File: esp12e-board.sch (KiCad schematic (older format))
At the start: 9 parts

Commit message: First version sent to fab
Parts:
- removed J?: Conn_02x05_Odd_Even, symbol Connector_Generic:Conn_02x05_Odd_Even
- removed J?: 5V AUX, Connector_PinSocket_2.54mm:PinSocket_1x02_P2.54mm_Vertical, symbol Connector:Conn_01x02_Female
- removed SW?: SW_Push, symbol Switch:SW_Push
- added J1: Header, Connector_PinHeader_2.54mm:PinHeader_2x08_P2.54mm_Vertical, symbol Connector_Generic:Conn_02x08_Odd_Even
- U2: renamed from U?; footprint (none) -> ESP8266:ESP-12E_SMD
- gave numbers to parts that had none: 5
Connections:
- wire segments 47 -> 55
- no-connect marks 11 -> 9

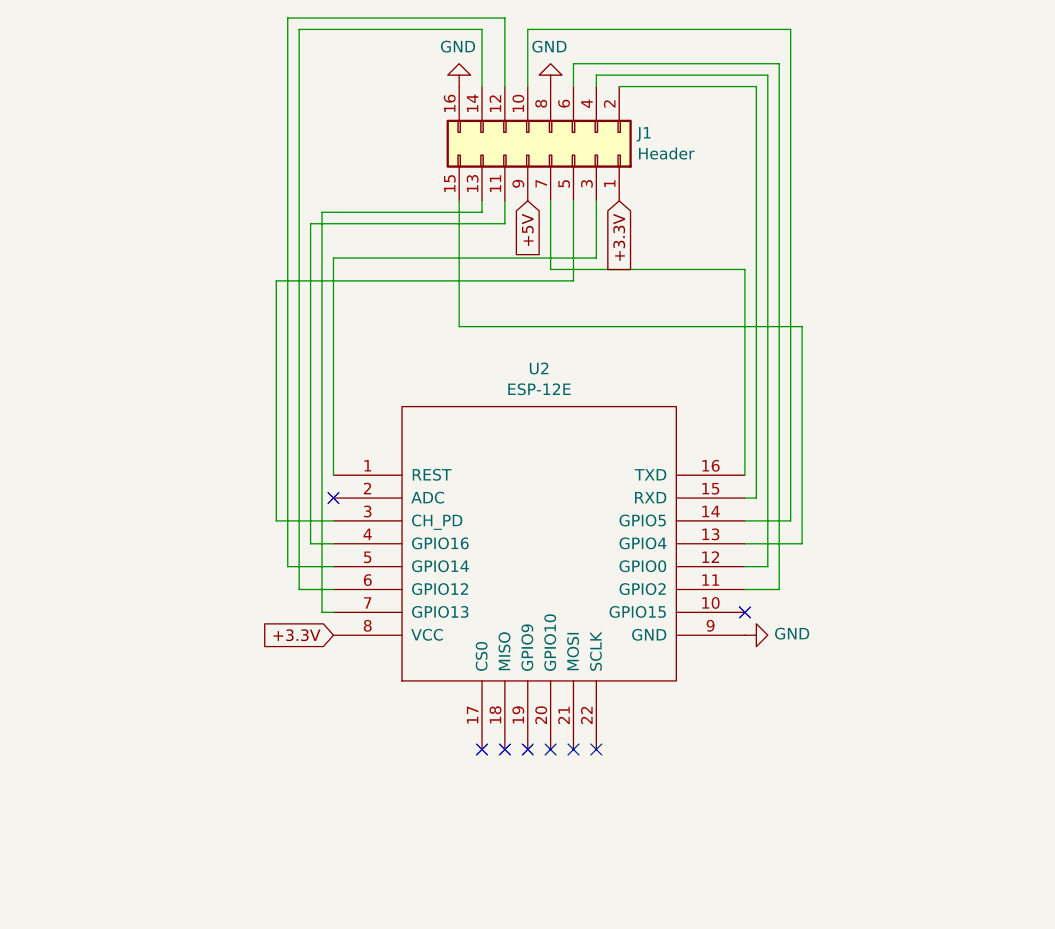
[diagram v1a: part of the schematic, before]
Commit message: adds necessary pull up/down resistors to pins to be able to boot
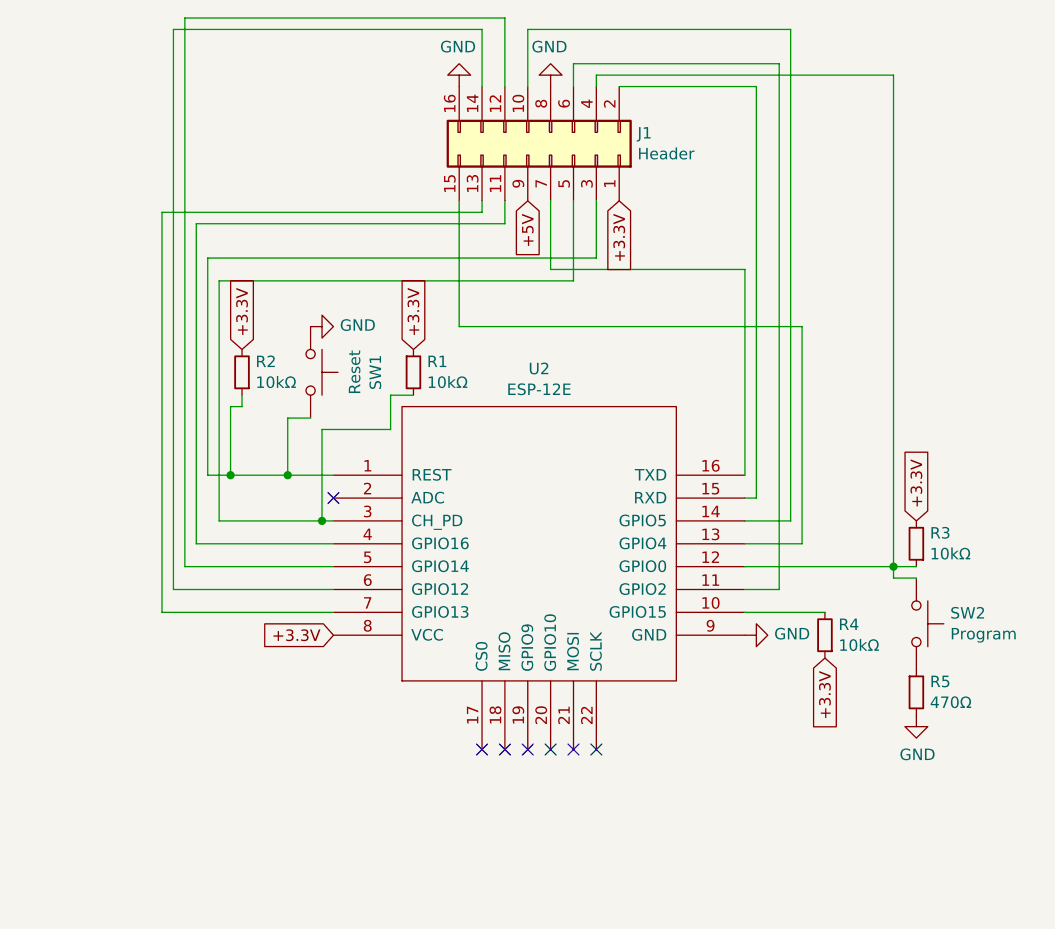
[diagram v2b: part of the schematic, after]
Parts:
- added R1, R2, R3, R4: 10kΩ, Resistor_SMD:R_0805_2012Metric_Pad1.15x1.40mm_HandSolder, symbol Device:R_Small
- added R5: 470Ω, Resistor_SMD:R_0805_2012Metric_Pad1.15x1.40mm_HandSolder, symbol Device:R_Small
- added SW1: Reset, Jumper:SolderJumper-2_P1.3mm_Open_RoundedPad1.0x1.5mm, symbol Switch:SW_Push
- added SW2: Program, Jumper:SolderJumper-2_P1.3mm_Open_RoundedPad1.0x1.5mm, symbol Switch:SW_Push
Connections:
- net +3.3V: now also R1.1, R2.2, R3.2, R4.1
- net GND: now also R5.2, SW1.1
- net at J1.3 (Pin_3), U2.1 (REST): now also R2.1, SW1.2
- net at U2.10 (GPIO15): now also R4.2
- net at J1.4 (Pin_4), U2.12 (GPIO0): now also R3.1, SW2.1
- net at J1.5 (Pin_5), U2.3 (CH_PD): now also R1.2
- new net: R5.1, SW2.2
- no-connect marks 9 -> 8
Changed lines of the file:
@@
 EESchema Schematic File Version 4
+LIBS:esp12e-board-cache
 EELAYER 30 0
 EELAYER END
@@
 NoConn ~ 5950 5150
 NoConn ~ 5850 5150
-NoConn ~ 6600 4550
 $Comp
 L ESP8266:ESP-12E U2
@@
 Wire Wire Line
 	6650 4050 6650 2250
-Wire Wire Line
-	4800 4250 4700 4250
 $Comp
 L power:GND #PWR01
@@
 +5V
 Wire Wire Line
-	4750 4550 4750 2800
-Wire Wire Line
-	4750 2800 5450 2800
-Wire Wire Line
 	5450 2800 5450 2750
 Wire Wire Line
-	4750 4550 4800 4550
-Wire Wire Line
 	5550 2750 5550 2850
 Wire Wire Line
-	5550 2850 4700 2850
-Wire Wire Line
-	4700 2850 4700 4250
-Wire Wire Line
 	6600 3050 5750 3050
 Wire Wire Line
@@
 	5450 2000 5450 2250
 Wire Wire Line
-	4650 2000 5450 2000
-Wire Wire Line
-	4650 4450 4650 2000
-Wire Wire Line
-	4800 4450 4650 4450
-Wire Wire Line
 	5550 1950 5550 2250
 Wire Wire Line
-	4600 1950 5550 1950
-Wire Wire Line
-	4600 4350 4600 1950
-Wire Wire Line
-	4800 4350 4600 4350
-Wire Wire Line
-	6600 4350 6700 4350
-Wire Wire Line
-	6700 4350 6700 2200
-Wire Wire Line
-	6700 2200 5950 2200
-Wire Wire Line
 	5950 2200 5950 2250
 Wire Wire Line
@@
 	5850 2150 5850 2250
 Wire Wire Line
-	4800 3950 4800 3000
-Wire Wire Line
-	4800 3000 5950 3000
-Wire Wire Line
 	5950 3000 5950 2750
 Wire Wire Line
-	4800 4150 4550 4150
-Wire Wire Line
-	4550 4150 4550 3100
-Wire Wire Line
-	4550 3100 5850 3100
-Wire Wire Line
 	5850 3100 5850 2750
 Wire Wire Line
@@
 Wire Wire Line
 	5350 3300 5350 2750
+$Comp
+L Device:R_Small R4
+U 1 1 5E563141
+P 6950 4650
+F 0 "R4" H 6891 4604 50  0000 R CNN
+F 1 "10kΩ" H 6891 4695 50  0000 R CNN
+F 2 "Resistor_SMD:R_0805_2012Metric_Pad1.15x1.40mm_HandSolder" H 6950 4650 50  0001 C CNN
+F 3 "~" H 6950 4650 50  0001 C CNN
+	1    6950 4650
+	-1   0    0    1
+$EndComp
+$Comp
+L Device:R_Small R3
+U 1 1 5E56376D
+P 7350 4250
+F 0 "R3" H 7291 4204 50  0000 R CNN
+F 1 "10kΩ" H 7291 4295 50  0000 R CNN
+F 2 "Resistor_SMD:R_0805_2012Metric_Pad1.15x1.40mm_HandSolder" H 7350 4250 50  0001 C CNN
+F 3 "~" H 7350 4250 50  0001 C CNN
+	1    7350 4250
+	-1   0    0    1
+$EndComp
+$Comp
+L Device:R_Small R2
+U 1 1 5E563C3F
+P 4400 3500
+F 0 "R2" H 4341 3454 50  0000 R CNN
+F 1 "10kΩ" H 4341 3545 50  0000 R CNN
+F 2 "Resistor_SMD:R_0805_2012Metric_Pad1.15x1.40mm_HandSolder" H 4400 3500 50  0001 C CNN
+F 3 "~" H 4400 3500 50  0001 C CNN
+	1    4400 3500
+	-1   0    0    1
+$EndComp
+Wire Wire Line
+	6600 4550 6950 4550
+Text GLabel 4400 3400 1    50   Input ~ 0
++3.3V
+Text GLabel 6950 4750 3    50   Input ~ 0
++3.3V
+Text GLabel 7350 4150 1    50   Input ~ 0
++3.3V
+Wire Wire Line
+	5950 2200 7250 2200
+Wire Wire Line
+	7250 4350 7250 2200
+$Comp
+L Device:R_Small R5
+U 1 1 5E5A201A
+P 7350 4900
+F 0 "R5" H 7409 4946 50  0000 L CNN
+F 1 "470Ω" H 7409 4855 50  0000 L CNN
+F 2 "Resistor_SMD:R_0805_2012Metric_Pad1.15x1.40mm_HandSolder" H 7350 4900 50  0001 C CNN
+F 3 "~" H 7350 4900 50  0001 C CNN
+	1    7350 4900
+	1    0    0    -1
+$EndComp
+Wire Wire Line
+	6600 4350 7250 4350
+Wire Wire Line
+	7250 4350 7350 4350
+Connection ~ 7250 4350
+Wire Wire Line
+	7250 4350 7250 4400
+Wire Wire Line
+	7250 4400 7350 4400
+$Comp
+L Switch:SW_Push SW2
+U 1 1 5E5AA7EE
+P 7350 4600
+F 0 "SW2" V 7304 4748 50  0000 L CNN
+F 1 "Program" V 7395 4748 50  0000 L CNN
+F 2 "Jumper:SolderJumper-2_P1.3mm_Open_RoundedPad1.0x1.5mm" H 7350 4800 50  0001 C CNN
+F 3 "~" H 7350 4800 50  0001 C CNN
+	1    7350 4600
+	0    1    1    0
+$EndComp
+$Comp
+L power:GND #PWR03
+U 1 1 5E5ADADC
+P 7350 5000
+F 0 "#PWR03" H 7350 4750 50  0001 C CNN
+F 1 "GND" H 7355 4827 50  0000 C CNN
+F 2 "" H 7350 5000 50  0001 C CNN
+F 3 "" H 7350 5000 50  0001 C CNN
+	1    7350 5000
+	1    0    0    -1
+$EndComp
+$Comp
+L Switch:SW_Push SW1
+U 1 1 5E5AE838
+P 4700 3500
+F 0 "SW1" H 4700 3785 50  0000 C CNN
+F 1 "Reset" H 4700 3694 50  0000 C CNN
+F 2 "Jumper:SolderJumper-2_P1.3mm_Open_RoundedPad1.0x1.5mm" H 4700 3700 50  0001 C CNN
+F 3 "~" H 4700 3700 50  0001 C CNN
+	1    4700 3500
+	0    1    1    0
+$EndComp
+Wire Wire Line
+	4750 4150 4800 4150
+Connection ~ 4750 4150
+Text GLabel 5150 3400 1    50   Input ~ 0
++3.3V
+$Comp
+L Device:R_Small R1
+U 1 1 5E5639CE
+P 5150 3500
+F 0 "R1" H 5209 3546 50  0000 L CNN
+F 1 "10kΩ" H 5209 3455 50  0000 L CNN
+F 2 "Resistor_SMD:R_0805_2012Metric_Pad1.15x1.40mm_HandSolder" H 5150 3500 50  0001 C CNN
+F 3 "~" H 5150 3500 50  0001 C CNN
+	1    5150 3500
+	1    0    0    -1
+$EndComp
+Wire Wire Line
+	4750 3750 4750 4150
+Wire Wire Line
+	4050 4550 4050 2800
+Wire Wire Line
+	4050 4550 4800 4550
+Wire Wire Line
+	4050 2800 5450 2800
+Wire Wire Line
+	4100 4450 4100 2000
+Wire Wire Line
+	4100 4450 4800 4450
+Wire Wire Line
+	4100 2000 5450 2000
+Wire Wire Line
+	4150 4350 4150 1950
+Wire Wire Line
+	4150 4350 4800 4350
+Wire Wire Line
+	4150 1950 5550 1950
+Wire Wire Line
+	4200 4250 4200 2850
+Wire Wire Line
+	4200 4250 4800 4250
+Wire Wire Line
+	4200 2850 5550 2850
+Wire Wire Line
+	4300 4150 4750 4150
+Wire Wire Line
+	4300 3100 5850 3100
+Wire Wire Line
+	4250 3950 4250 3000
+Wire Wire Line
+	4250 3000 5950 3000
+Wire Wire Line
+	4250 3950 4350 3950
+$Comp
+L power:GND #PWR02
+U 1 1 5E5DA0BD
+P 4700 3300
+F 0 "#PWR02" H 4700 3050 50  0001 C CNN
+F 1 "GND" V 4705 3172 50  0000 R CNN
+F 2 "" H 4700 3300 50  0001 C CNN
+F 3 "" H 4700 3300 50  0001 C CNN
+	1    4700 3300
+	0    -1   -1   0
+$EndComp
+Wire Wire Line
+	4300 3100 4300 4150
+Wire Wire Line
+	4400 3600 4400 3650
+Wire Wire Line
+	4400 3650 4350 3650
+Wire Wire Line
+	4350 3650 4350 3950
+Connection ~ 4350 3950
+Wire Wire Line
+	4350 3950 4600 3950
+Wire Wire Line
+	5050 3750 5050 3600
+Wire Wire Line
+	5050 3600 5150 3600
+Wire Wire Line
+	4750 3750 5050 3750
+Wire Wire Line
+	4700 3700 4600 3700
+Wire Wire Line
+	4600 3700 4600 3950
+Connection ~ 4600 3950
+Wire Wire Line
+	4600 3950 4800 3950
 $EndSCHEMATC

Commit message: rewiring and changed pads to switches
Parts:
- SW1, SW2: footprint Jumper:SolderJumper-2_P1.3mm_Open_RoundedPad1.0x1.5mm -> Button_Switch_THT:SW_DIP_SPSTx01_Slide_6.7x4.1mm_W7.62mm_P2.54mm_LowProfile
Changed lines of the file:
@@
 F 0 "SW2" V 7304 4748 50  0000 L CNN
 F 1 "Program" V 7395 4748 50  0000 L CNN
-F 2 "Jumper:SolderJumper-2_P1.3mm_Open_RoundedPad1.0x1.5mm" H 7350 4800 50  0001 C CNN
+F 2 "Button_Switch_THT:SW_DIP_SPSTx01_Slide_6.7x4.1mm_W7.62mm_P2.54mm_LowProfile" H 7350 4800 50  0001 C CNN
 F 3 "~" H 7350 4800 50  0001 C CNN
 	1    7350 4600
@@
 F 0 "SW1" H 4700 3785 50  0000 C CNN
 F 1 "Reset" H 4700 3694 50  0000 C CNN
-F 2 "Jumper:SolderJumper-2_P1.3mm_Open_RoundedPad1.0x1.5mm" H 4700 3700 50  0001 C CNN
+F 2 "Button_Switch_THT:SW_DIP_SPSTx01_Slide_6.7x4.1mm_W7.62mm_P2.54mm_LowProfile" H 4700 3700 50  0001 C CNN
 F 3 "~" H 4700 3700 50  0001 C CNN
 	1    4700 3500

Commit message: replaces buttons with THT ones
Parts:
- SW1, SW2: footprint Button_Switch_THT:SW_DIP_SPSTx01_Slide_6.7x4.1mm_W7.62mm_P2.54mm_LowProfile -> Button_Switch_SMD:SW_SPST_B3U-1000P-B
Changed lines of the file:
@@
 F 0 "SW2" V 7304 4748 50  0000 L CNN
 F 1 "Program" V 7395 4748 50  0000 L CNN
-F 2 "Button_Switch_THT:SW_DIP_SPSTx01_Slide_6.7x4.1mm_W7.62mm_P2.54mm_LowProfile" H 7350 4800 50  0001 C CNN
+F 2 "Button_Switch_SMD:SW_SPST_B3U-1000P-B" H 7350 4800 50  0001 C CNN
 F 3 "~" H 7350 4800 50  0001 C CNN
 	1    7350 4600
@@
 F 0 "SW1" H 4700 3785 50  0000 C CNN
 F 1 "Reset" H 4700 3694 50  0000 C CNN
-F 2 "Button_Switch_THT:SW_DIP_SPSTx01_Slide_6.7x4.1mm_W7.62mm_P2.54mm_LowProfile" H 4700 3700 50  0001 C CNN
+F 2 "Button_Switch_SMD:SW_SPST_B3U-1000P-B" H 4700 3700 50  0001 C CNN
 F 3 "~" H 4700 3700 50  0001 C CNN
 	1    4700 3500

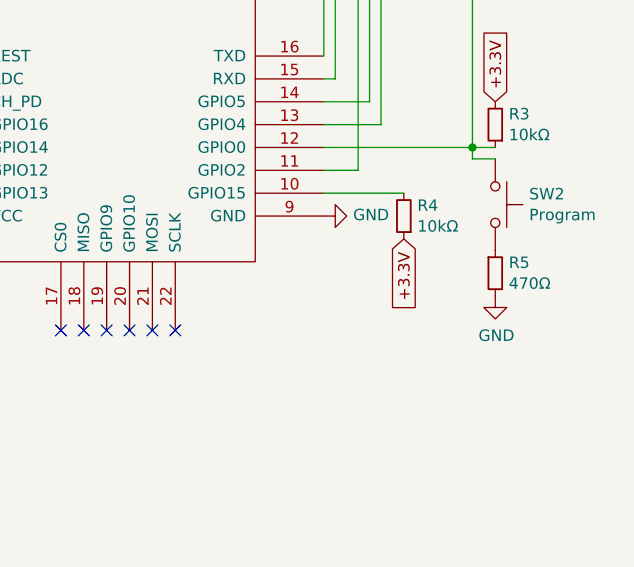
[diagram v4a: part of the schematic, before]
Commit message: fixes booting - io15 should be pulled down
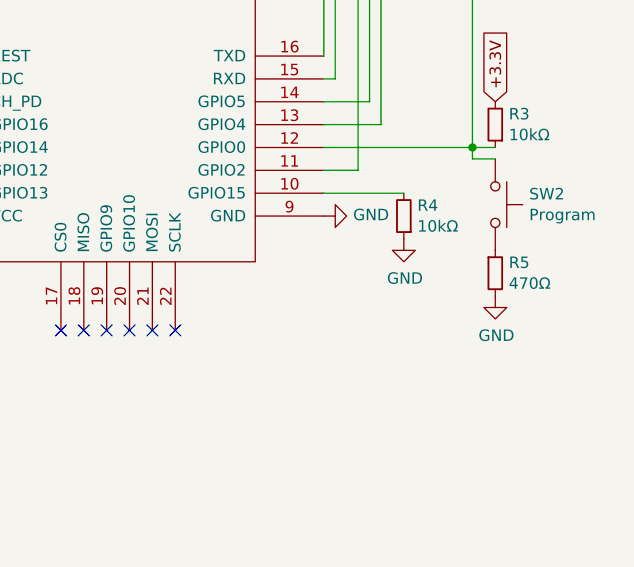
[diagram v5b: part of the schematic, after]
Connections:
- net +3.3V: no longer R4.1
- net GND: now also R4.1
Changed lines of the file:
@@
 Text GLabel 4400 3400 1    50   Input ~ 0
-+3.3V
-Text GLabel 6950 4750 3    50   Input ~ 0
 +3.3V
 Text GLabel 7350 4150 1    50   Input ~ 0
@@
 Wire Wire Line
 	4600 3950 4800 3950
+$Comp
+L power:GND #PWR?
+U 1 1 5E93358B
+P 6950 4750
+F 0 "#PWR?" H 6950 4500 50  0001 C CNN
+F 1 "GND" H 6955 4577 50  0000 C CNN
+F 2 "" H 6950 4750 50  0001 C CNN
+F 3 "" H 6950 4750 50  0001 C CNN
+	1    6950 4750
+	1    0    0    -1
+$EndComp
 $EndSCHEMATC
